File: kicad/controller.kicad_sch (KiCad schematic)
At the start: 23 parts, among them M5 Motor_DC, M6 Motor_DC, M7 Motor_DC, M8 Motor_DC, U10 DRV8833PW, U6 ESP32-DEVKITC, U8 GY-521

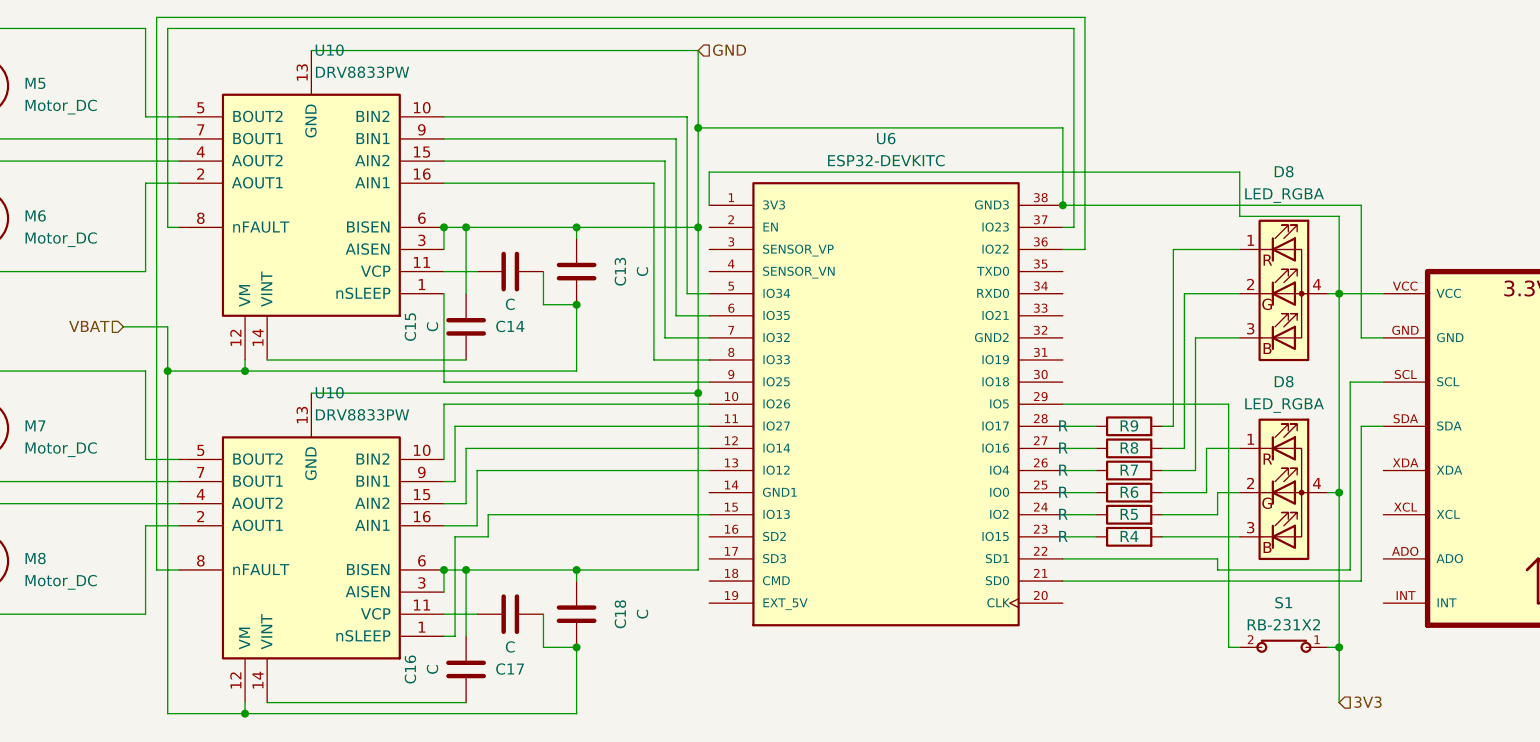
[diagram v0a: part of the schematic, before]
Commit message: Add all symbols and values
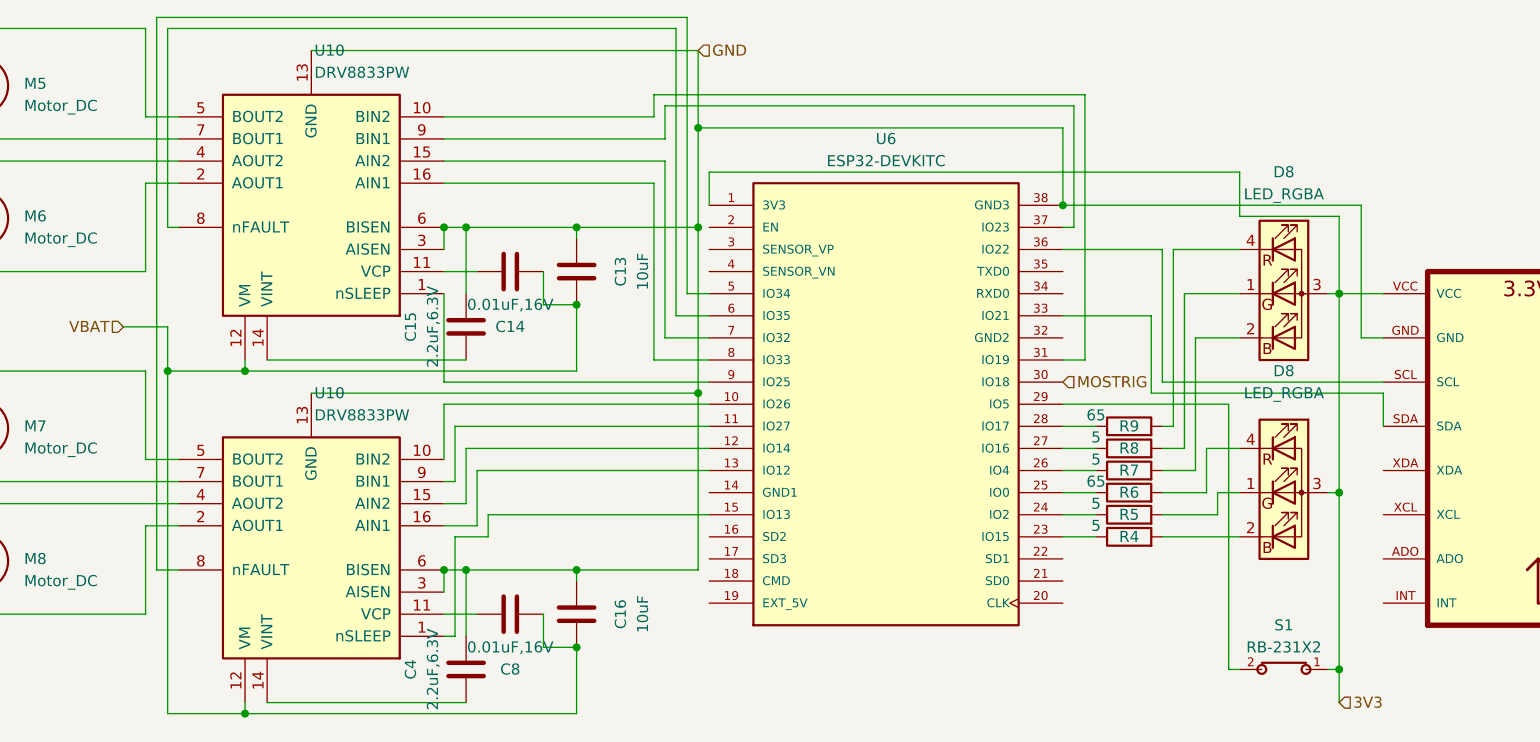
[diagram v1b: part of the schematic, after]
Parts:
- removed C17, C18: C, symbol Device:C
- added C4: 2.2uF,6.3V, Capacitor_SMD:C_0805_2012Metric, symbol Device:C
- added C8: 0.01uF,16V, Capacitor_SMD:C_0805_2012Metric, symbol Device:C
- C13, C16: value C -> 10uF; footprint (none) -> Capacitor_SMD:C_0805_2012Metric
- C14: value C -> 0.01uF,16V; footprint (none) -> Capacitor_SMD:C_0805_2012Metric
- C15: value C -> 2.2uF,6.3V; footprint (none) -> Capacitor_SMD:C_0805_2012Metric
- D8: footprint (none) -> Connector_PinHeader_1.00mm:PinHeader_1x04_P1.00mm_Vertical
- M5, M6, M7, M8: footprint (none) -> Connector_PinSocket_2.54mm:PinSocket_1x02_P2.54mm_Vertical
- R4, R5, R7, R8: value R -> 5; footprint (none) -> Resistor_SMD:R_0805_2012Metric
- R6, R9: value R -> 65; footprint (none) -> Resistor_SMD:R_0805_2012Metric
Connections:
- net 3V3: now also D8.3 (A), D8.3 (A); no longer D8.4 (A), D8.4 (A)
- net GND: now also C4.1
- net VBAT: now also C16.2, C8.2
- net at U10.14 (VINT): now also C4.2; no longer C16.2
- net at R4.2: now also D8.2 (BK); no longer D8.3 (BK)
- net at R8.2: now also D8.1 (GK); no longer D8.2 (GK)
- net at R6.2: now also D8.4 (RK); no longer D8.1 (RK)
- net at U10.10 (BIN2): now also U6.31 (IO19); no longer U6.5 (IO34)
- net at U10.8 (nFAULT): now also U6.6 (IO35); no longer U6.37 (IO23)
- net at U10.9 (BIN1): now also U6.37 (IO23); no longer U6.6 (IO35)
- net at R9.2: now also D8.4 (RK); no longer D8.1 (RK)
- net at R7.2: now also D8.2 (BK); no longer D8.3 (BK)
- net at U10.11 (VCP): now also C8.1
- net at R5.2: now also D8.1 (GK); no longer D8.2 (GK)
- net at U8.SCL: now also U6.36 (IO22); no longer U6.22 (SD1)
- net at U8.SDA: now also U6.33 (IO21); no longer U6.21 (SD0)
- net MOSTRIG: now reaches U6.30 (IO18)
- net at U10.8 (nFAULT): now also U6.5 (IO34); no longer U6.36 (IO22)
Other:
- moved on the sheet: S1

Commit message: Fix footprints
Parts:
- U6: footprint ESP32-DEVKITC:MODULE_ESP32-DEVKITC -> ESP32-DEVKIT:MODULE_ESP32-DEVKITC
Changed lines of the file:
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@@
       (effects (font (size 1.27 1.27)))
     )
-    (property "Footprint" "ESP32-DEVKITC:MODULE_ESP32-DEVKITC" (at 161.29 107.95 0)
+    (property "Footprint" "ESP32-DEVKIT:MODULE_ESP32-DEVKITC" (at 161.29 107.95 0)
       (effects (font (size 1.27 1.27)) (justify bottom) hide)
     )

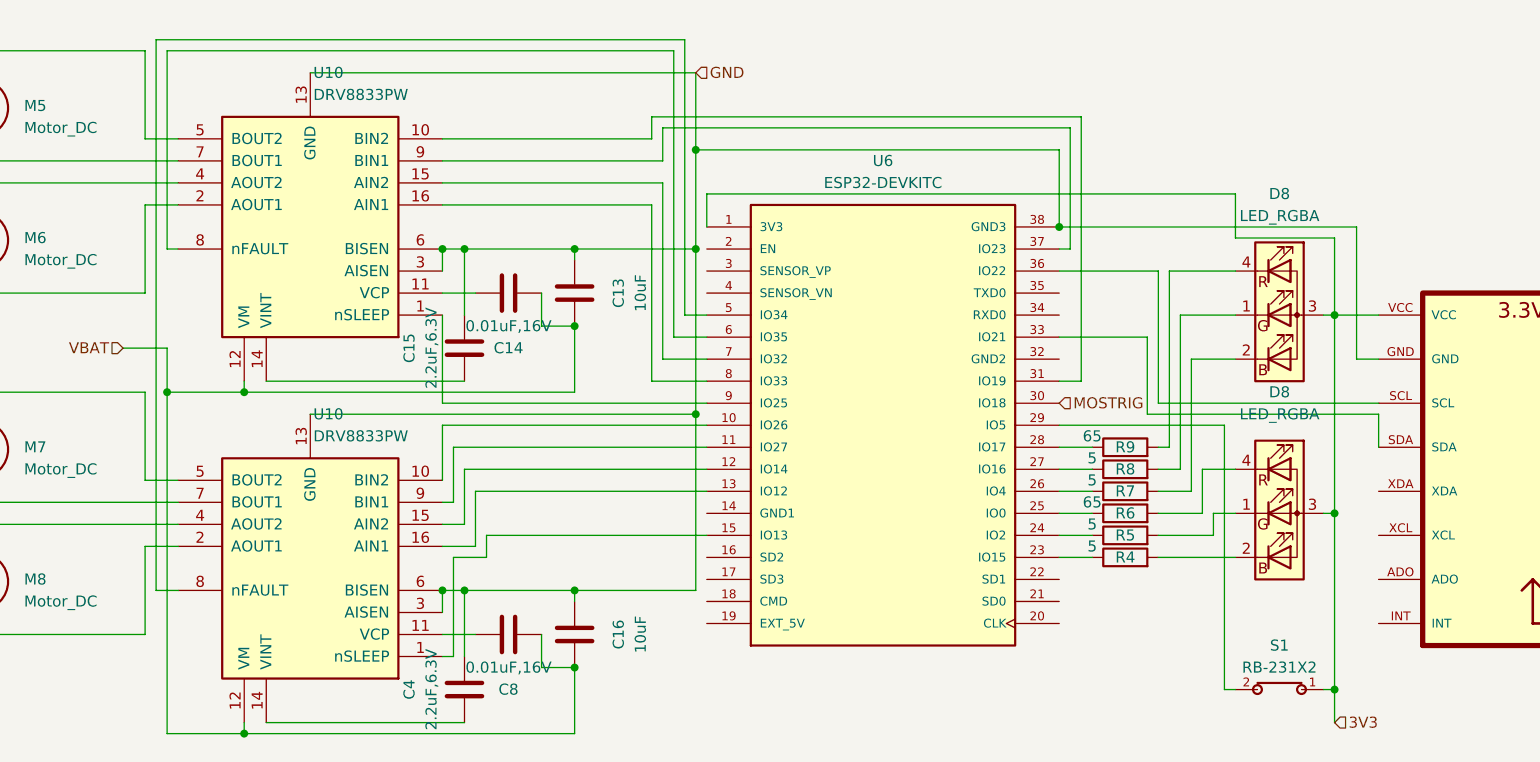
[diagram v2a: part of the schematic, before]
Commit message: Add board layout
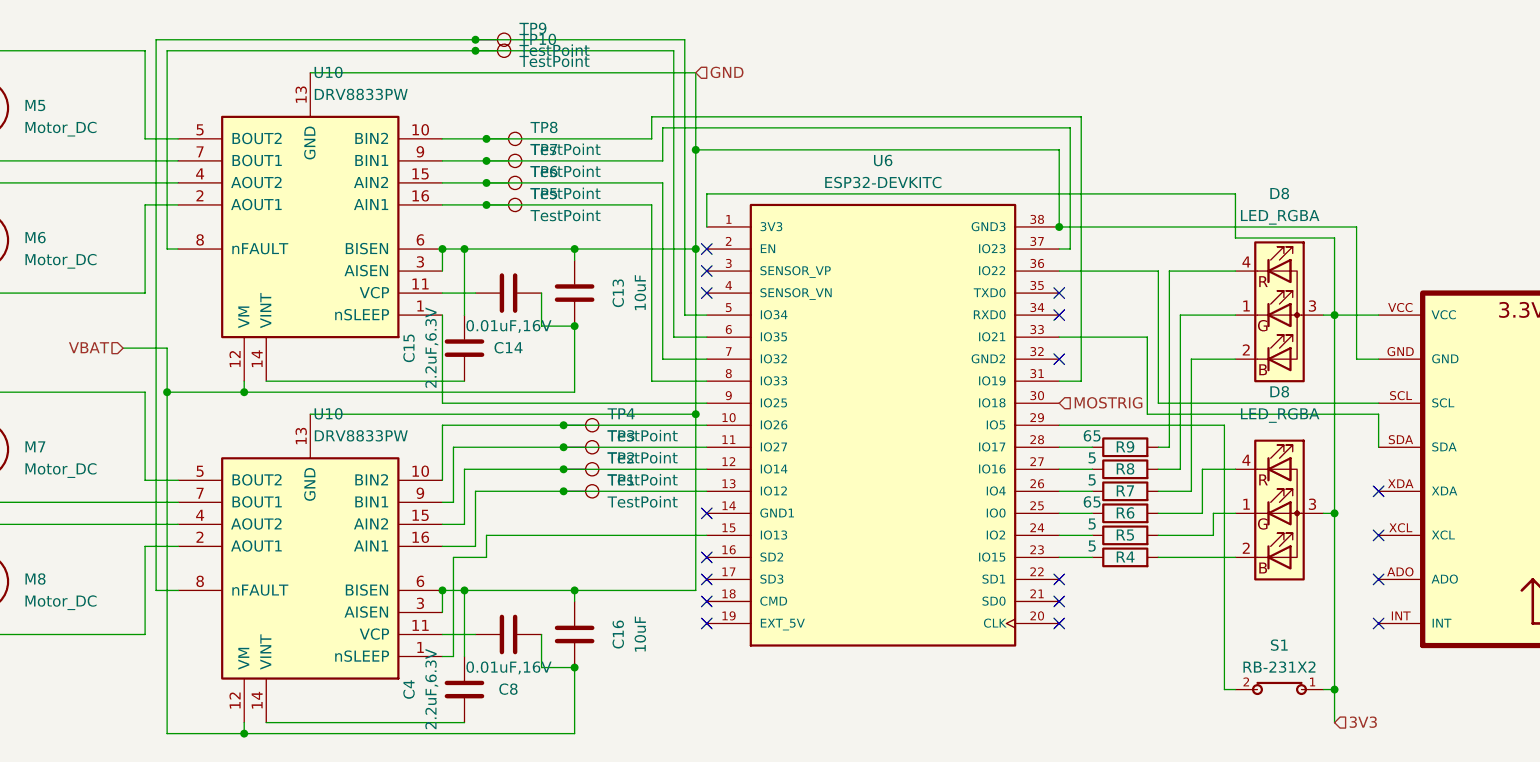
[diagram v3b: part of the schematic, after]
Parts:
- added TP1, TP10, TP2, TP3, TP4, TP5, TP6, TP7, TP8, TP9: TestPoint, TestPoint:TestPoint_Pad_D2.0mm, symbol Connector:TestPoint
- C13, C14, C15, C16, C4, C8: footprint Capacitor_SMD:C_0805_2012Metric -> Capacitor_SMD:C_0805_2012Metric_Pad1.18x1.45mm_HandSolder
- R4, R5, R6, R7, R8, R9: footprint Resistor_SMD:R_0805_2012Metric -> Resistor_SMD:R_0805_2012Metric_Pad1.20x1.40mm_HandSolder
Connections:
- net at U10.10 (BIN2), U6.31 (IO19): now also TP8.1
- net at U10.15 (AIN2), U6.7 (IO32): now also TP6.1
- net at U10.16 (AIN1), U6.8 (IO33): now also TP5.1
- net at U10.8 (nFAULT), U6.6 (IO35): now also TP10.1
- net at U10.9 (BIN1), U6.37 (IO23): now also TP7.1
- net at U10.10 (BIN2), U6.10 (IO26): now also TP4.1
- net at U10.9 (BIN1), U6.11 (IO27): now also TP3.1
- net at U10.15 (AIN2), U6.12 (IO14): now also TP2.1
- net at U10.16 (AIN1), U6.13 (IO12): now also TP1.1
- net at U10.8 (nFAULT), U6.5 (IO34): now also TP9.1
- no-connect marks 0 -> 18

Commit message: So many DRC errors
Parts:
- D8: footprint Connector_PinHeader_1.00mm:PinHeader_1x04_P1.00mm_Vertical -> Connector_PinSocket_2.54mm:PinSocket_1x04_P2.54mm_Vertical
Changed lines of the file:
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@@
       (effects (font (size 1.27 1.27)))
     )
-    (property "Footprint" "Connector_PinHeader_1.00mm:PinHeader_1x04_P1.00mm_Vertical" (at 207.01 96.52 0)
+    (property "Footprint" "Connector_PinSocket_2.54mm:PinSocket_1x04_P2.54mm_Vertical" (at 207.01 96.52 0)
       (effects (font (size 1.27 1.27)) hide)
     )
@@
       (effects (font (size 1.27 1.27)))
     )
-    (property "Footprint" "Connector_PinHeader_1.00mm:PinHeader_1x04_P1.00mm_Vertical" (at 207.01 119.38 0)
+    (property "Footprint" "Connector_PinSocket_2.54mm:PinSocket_1x04_P2.54mm_Vertical" (at 207.01 119.38 0)
       (effects (font (size 1.27 1.27)) hide)
     )
